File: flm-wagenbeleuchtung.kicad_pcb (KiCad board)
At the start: 2 copper layers, 153 x 9.4 mm, 31 parts

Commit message: v2
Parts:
- added C5: 200u, Capacitor_Tantalum_SMD:CP_EIA-7343-31_Kemet-D_Pad2.25x2.55mm_HandSolder, F.Cu at (128.4, 124.7)
- added C6: 200u, Capacitor_Tantalum_SMD:CP_EIA-7343-31_Kemet-D_Pad2.25x2.55mm_HandSolder, F.Cu at (156.9, 124.7)
- moved D32 25.5 mm to (71.7, 124.7), turned to -90 degrees
- moved D42 25.3 mm to (221.1, 124.7), turned to -90 degrees
- moved D31 18.9 mm to (87.0, 120.7)
- moved D43 18.7 mm to (205.9, 128.7)
- moved D33 15.8 mm to (87.0, 128.7), turned to 0 degrees
- moved D41 15.7 mm to (205.9, 120.9), turned to 0 degrees
- moved D23 12.2 mm to (101.5, 124.7)
- moved D1 12.1 mm to (191.5, 124.7)
- moved R4 10.1 mm to (95.5, 127.9)
- moved D22 9.14 mm to (112.8, 124.7)
- moved D2 9.09 mm to (180.2, 124.7)
- moved C1 8.15 mm to (171.2, 124.7)
- moved D21 6.10 mm to (124.0, 124.7)
- moved D3 6.05 mm to (169.0, 124.7)
- moved C4 5.92 mm to (114.1, 124.7)
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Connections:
- RV1 pad 3: GND -> unconnected-(RV1-Pad3)
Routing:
- net Net-(D33-Pad2): track 34.2 -> 5.74 mm
- net Net-(D43-Pad2): track 3.57 -> 18.9 mm
- net Net-(D41-Pad2): track 29.2 -> 14.8 mm
- net Net-(D32-Pad2): track 28.7 -> 16.0 mm
- net Net-(D23-Pad2): track 3.41 -> 13.9 mm
- net Net-(D31-Pad2): track 5.64 -> 16.0 mm
- net Net-(D42-Pad2): track 5.64 -> 15.7 mm
- net GND: track 250.5 -> 260.3 mm
- net VCC: track 169.5 -> 178.2 mm
- net Net-(D3-Pad2): track 3.39 -> 7.74 mm
- net Net-(D21-Pad2): track 5.64 -> 8.67 mm
- net Net-(D22-Pad2): track 5.64 -> 8.67 mm
- net Net-(D2-Pad2): track 5.64 -> 8.67 mm
- net Net-(D12-Pad2): track 5.64 -> 8.67 mm
- net Net-(D1-Pad2): track 5.64 -> 8.67 mm
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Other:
- board size 153 x 9.4 mm -> 153 x 10.4 mm
- board text added: "FLM-Wagenbeleuchtung v2"
- board text added: "Pufferkondensatoren C1-C6: 16 V / 100u oder mehr"
- board text removed: "Pufferkondensatoren C1-C4: 16 V / 100u oder mehr"

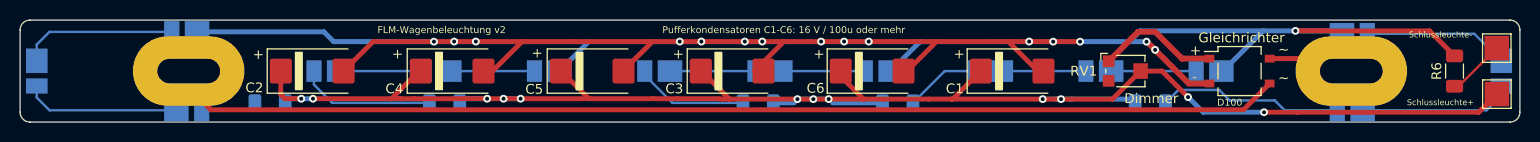
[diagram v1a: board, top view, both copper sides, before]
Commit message: lochabstand etwas größer, damit auch restaurantwagen passen
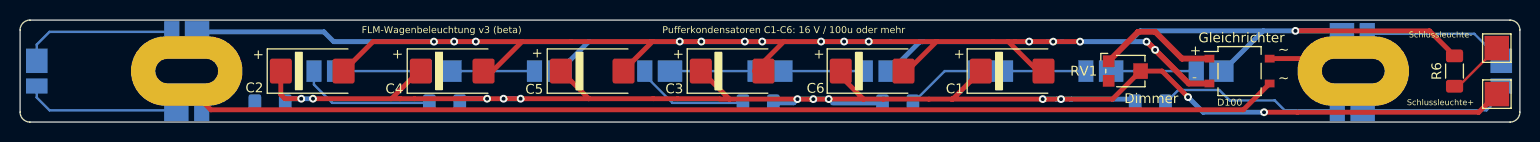
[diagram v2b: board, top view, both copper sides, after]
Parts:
- moved REF** 0.20 mm to (207.7, 124.7)
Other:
- board text added: "FLM-Wagenbeleuchtung v3 (beta)"
- board text removed: "FLM-Wagenbeleuchtung v2"
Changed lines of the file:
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@@
       (effects (font (size 1 1) (thickness 0.15)))
     )
-    (pad "1" thru_hole oval (at 1.7 0) (size 11.4 7.1) (drill oval 6.4 2.5) (layers *.Cu "F.Mask") (remove_unused_layers)
+    (pad "1" thru_hole oval (at 1.5 0) (size 11.4 7.1) (drill oval 6.4 2.5) (layers *.Cu "F.Mask") (remove_unused_layers)
       (net 3 "/TRACK_P"))
   )
@@
   )
   (footprint "JS_Local:Fleischmann_Waggon_Pad" (layer "F.Cu")
-    (at 207.5 124.7)
+    (at 207.7 124.7)
     (attr smd)
     (fp_text reference "REF**" (at 0 -0.5 unlocked) (layer "F.SilkS") hide
@@
     (effects (font (size 1 1) (thickness 0.15)))
   )
-  (gr_text "FLM-Wagenbeleuchtung v2" (at 113 120.5) (layer "F.SilkS")
+  (gr_text "FLM-Wagenbeleuchtung v3 (beta)" (at 113 120.5) (layer "F.SilkS")
     (effects (font (size 0.7 0.7) (thickness 0.1)))
   )
